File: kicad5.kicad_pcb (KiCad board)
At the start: 2 copper layers, 7 parts, among them SW1 SW_Push, SW2 SW_Push, SW3 SW_Push, SW4 SW_Push, U1 XIAO-RP2040-DIP

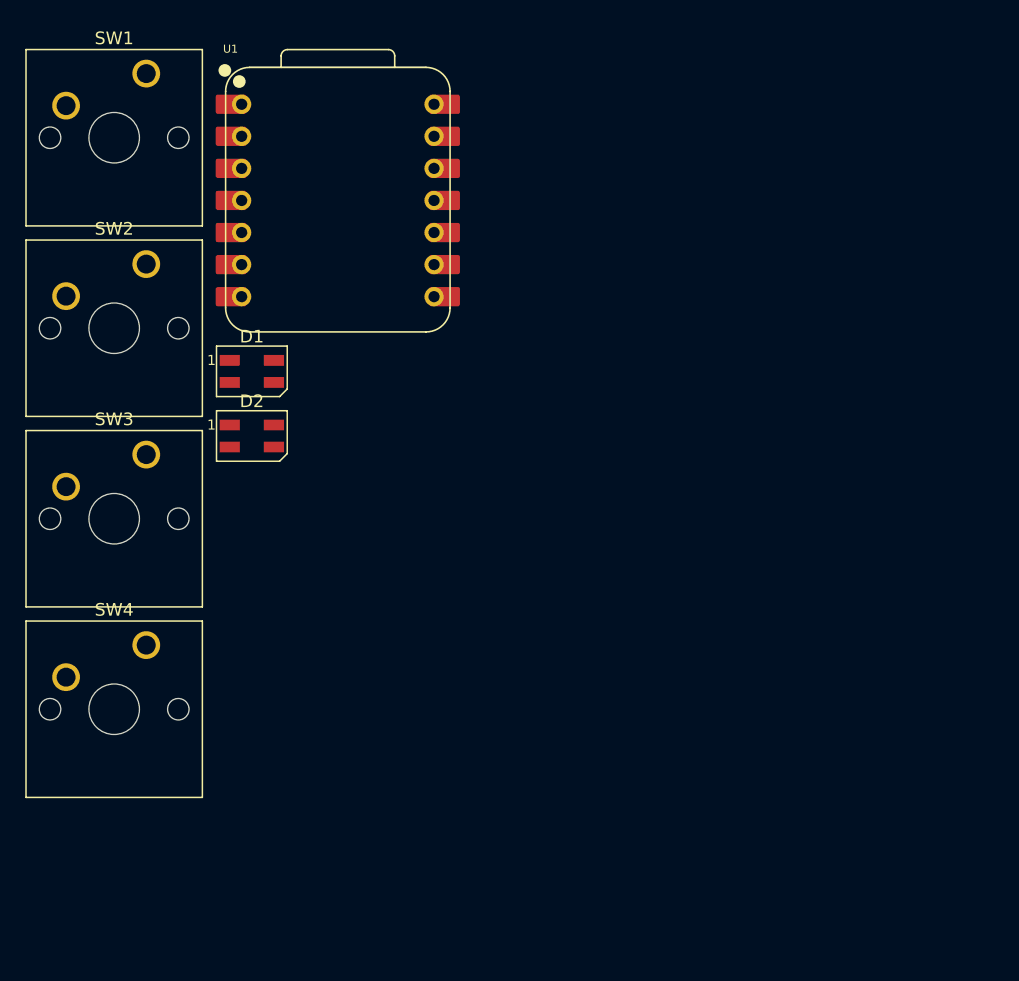
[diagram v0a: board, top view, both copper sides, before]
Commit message: added ec11
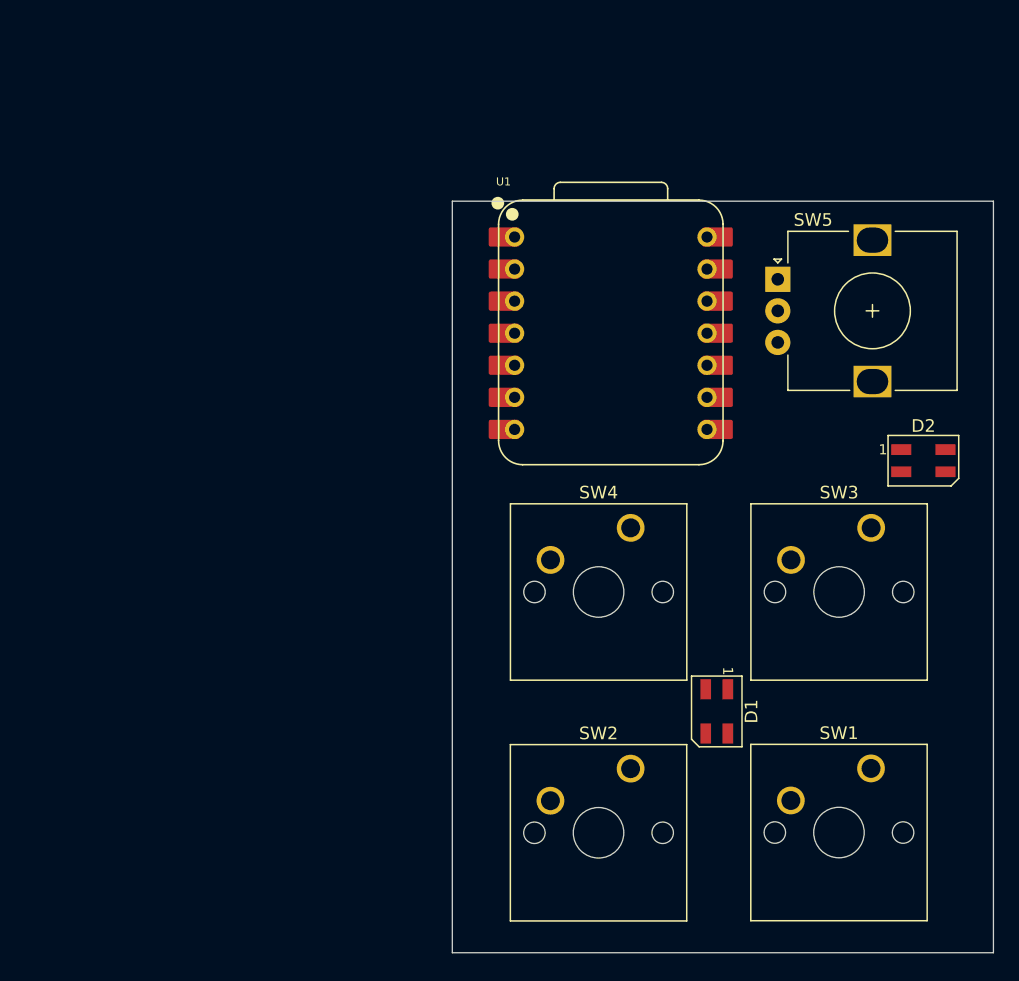
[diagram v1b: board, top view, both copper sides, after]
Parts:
- added SW5: RotaryEncoder_Switch, ec11:RotaryEncoder_Alps_EC12E_Vertical_H20mm, F.Cu at (163.9, 77.6)
- moved SW1 79.5 mm to (171.3, 116.4)
- moved SW3 57.7 mm to (171.3, 97.3)
- moved SW2 55.4 mm to (152.2, 116.4)
- moved D2 53.2 mm to (175.4, 92.0)
- moved D1 45.6 mm to (159.1, 111.9), turned to -90 degrees
- moved SW4 39.5 mm to (152.2, 97.3)
- moved U1 24.0 mm to (150.7, 81.9)
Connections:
- U1 pad 1: unconnected-(U1-GPIO26/ADC0/A0-Pad1) -> Net-(U1-GPIO26/ADC0/A0)
- U1 pad 2: unconnected-(U1-GPIO27/ADC1/A1-Pad2) -> Net-(U1-GPIO27/ADC1/A1)
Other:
- board outline added: 42.9 x 59.5 mm

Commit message: PCB routing is done
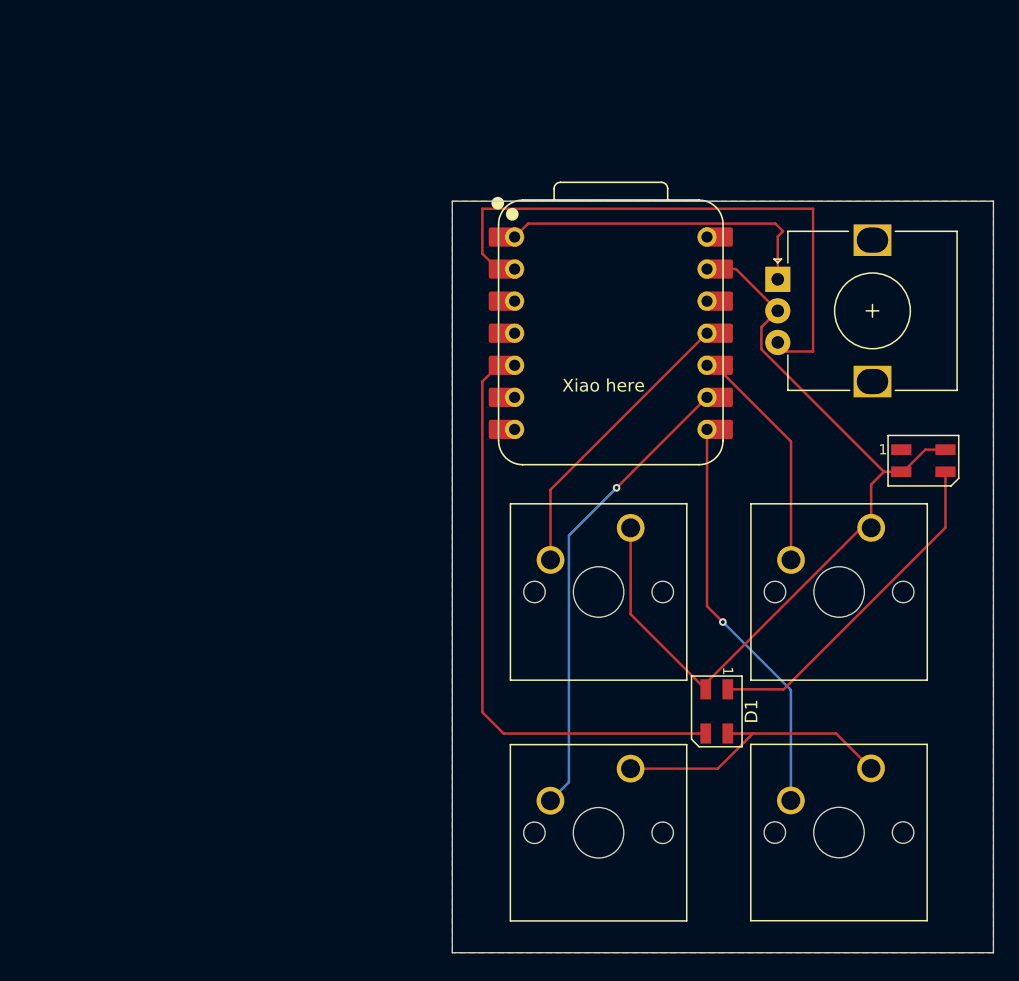
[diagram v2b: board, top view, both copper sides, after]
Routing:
- net GND: track 0.00 -> 92.0 mm
- net Net-(D1-DIN): track 0.00 -> 47.7 mm
- net Net-(U1-GPIO27/ADC1/A1): track 0.00 -> 47.2 mm
- net Net-(U1-GPIO2/SCK): track 0.00 -> 37.9 mm, vias 0 -> 1
- net Net-(U1-GPIO1/RX): track 0.00 -> 32.1 mm, vias 0 -> 1
- net Net-(D1-DOUT): track 0.00 -> 27.0 mm
- net Net-(U1-GPIO26/ADC0/A0): track 0.00 -> 25.9 mm
- net Net-(U1-GPIO3/MOSI): track 0.00 -> 23.1 mm
- net Net-(U1-GPIO4/MISO): track 0.00 -> 18.5 mm
- added copper zone on F.Cu, net GND
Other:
- board text added: "A's Hackpad"
- board text added: "Xiao here"

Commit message: Added case model
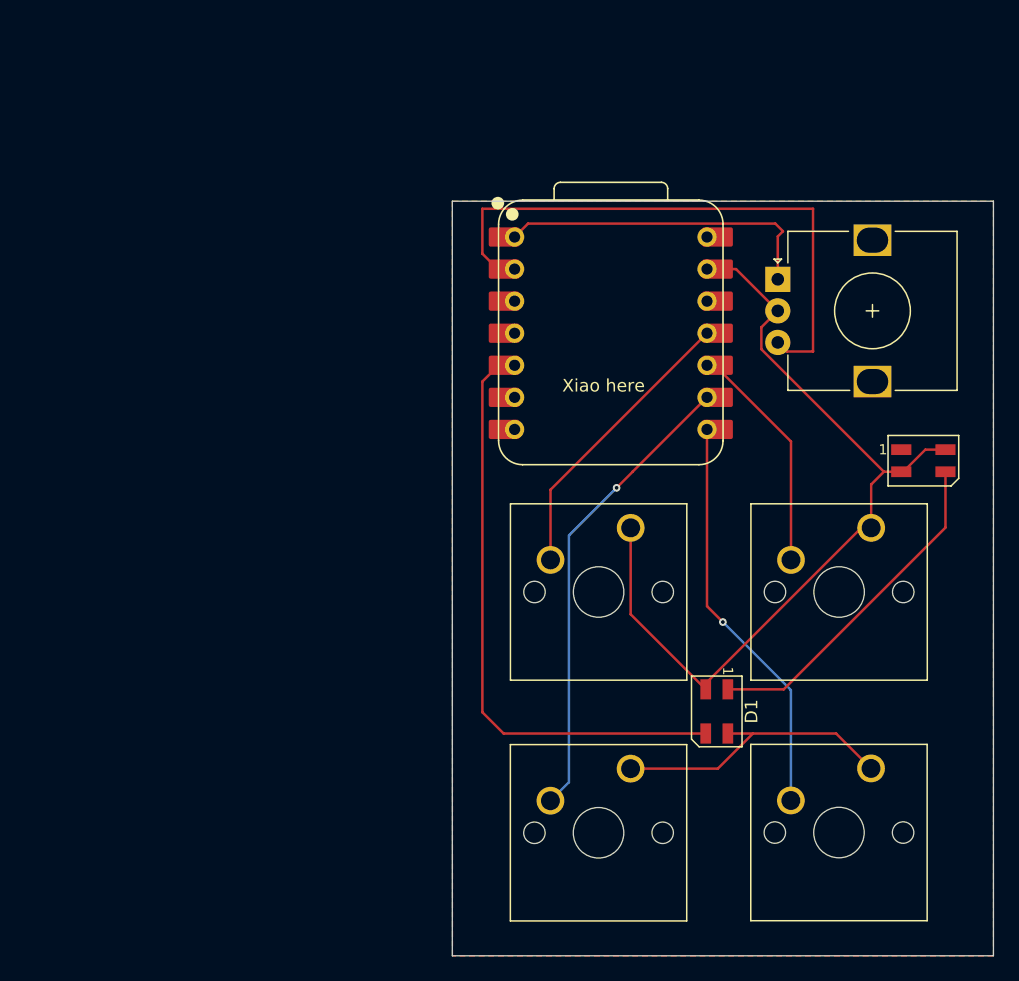
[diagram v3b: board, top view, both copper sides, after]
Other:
- board size 42.9 x 59.5 mm -> 42.9 x 59.8 mm
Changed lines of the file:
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@@
 	(gr_rect
 		(start 138.1125 71.4375)
-		(end 180.975 130.96875)
+		(end 180.975 131.210328)
 		(stroke
 			(width 0.05)
@@
 		(min_thickness 0.25)
 		(filled_areas_thickness no)
-		(fill yes
+		(fill
 			(thermal_gap 0.5)
 			(thermal_bridge_width 0.5)
@@
 		(polygon
 			(pts
-				(xy 180.975 71.4375) (xy 180.975 130.96875) (xy 138.1125 130.96875) (xy 138.1125 71.4375)
+				(xy 180.975 71.4375) (xy 180.975 131.221852) (xy 138.124999 131.224977) (xy 138.1125 71.4375)
 			)
 		)
